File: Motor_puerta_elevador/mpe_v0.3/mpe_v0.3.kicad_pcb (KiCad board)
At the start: 2 copper layers, 99.7 x 109.9 mm, 50 parts, among them J1 IBT2, J10 ENCODER, J11 SERIAL, J12 POWER, J13 MOTOR, J15 -, J16 -, J2 POWER, J3 MOTOR, J4 PROG, J5 IN1, J6 IN2, J7 IN3, J8 IN4, J9 IN5, P1 Power, P2 Analog, P3 Digital, P4 Digital, P6 CONN_01X01, P7 CONN_01X01, SW1 RESET, U1 ATmega3250PA-AU, U2 PC817, U3 PC817, U4 PC817, U5 PC817, U6 PC817, U7 DCDC_StepDown, Y1 16M

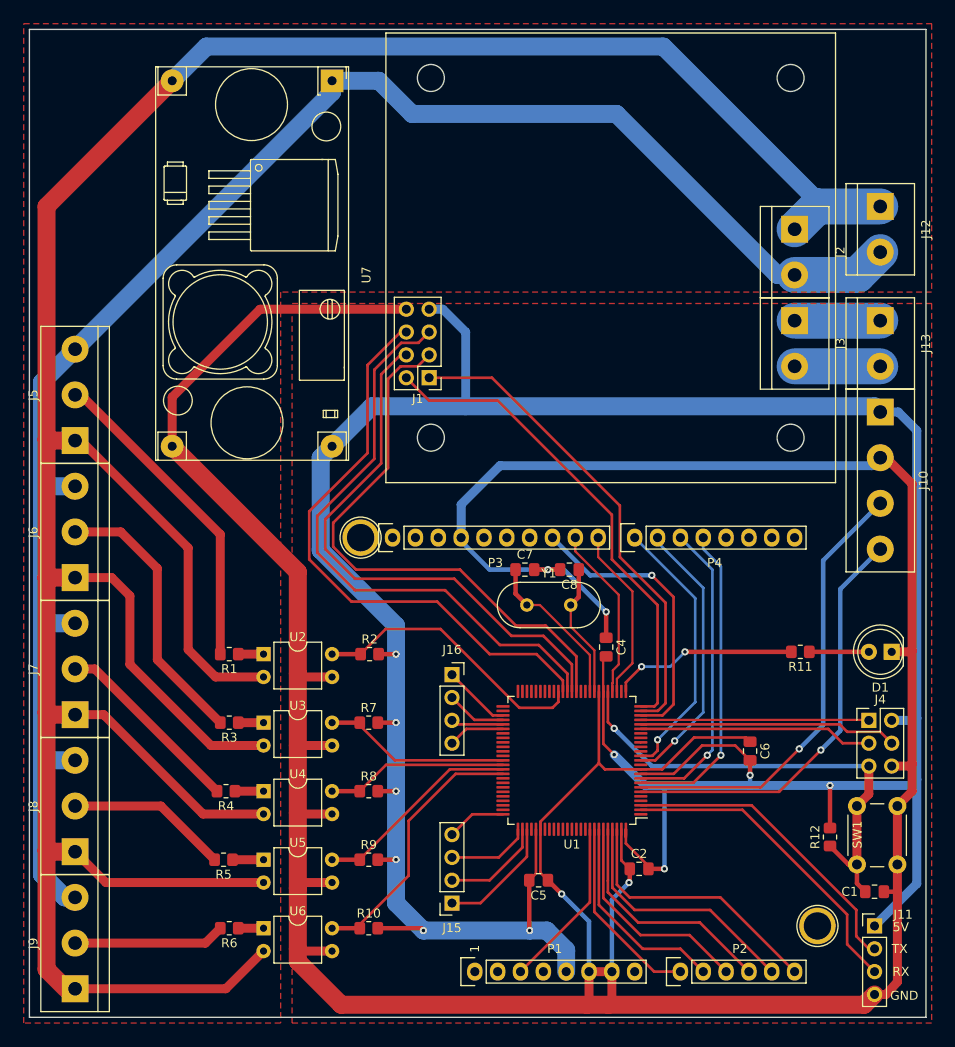
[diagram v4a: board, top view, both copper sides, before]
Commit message: poner zonas relleno
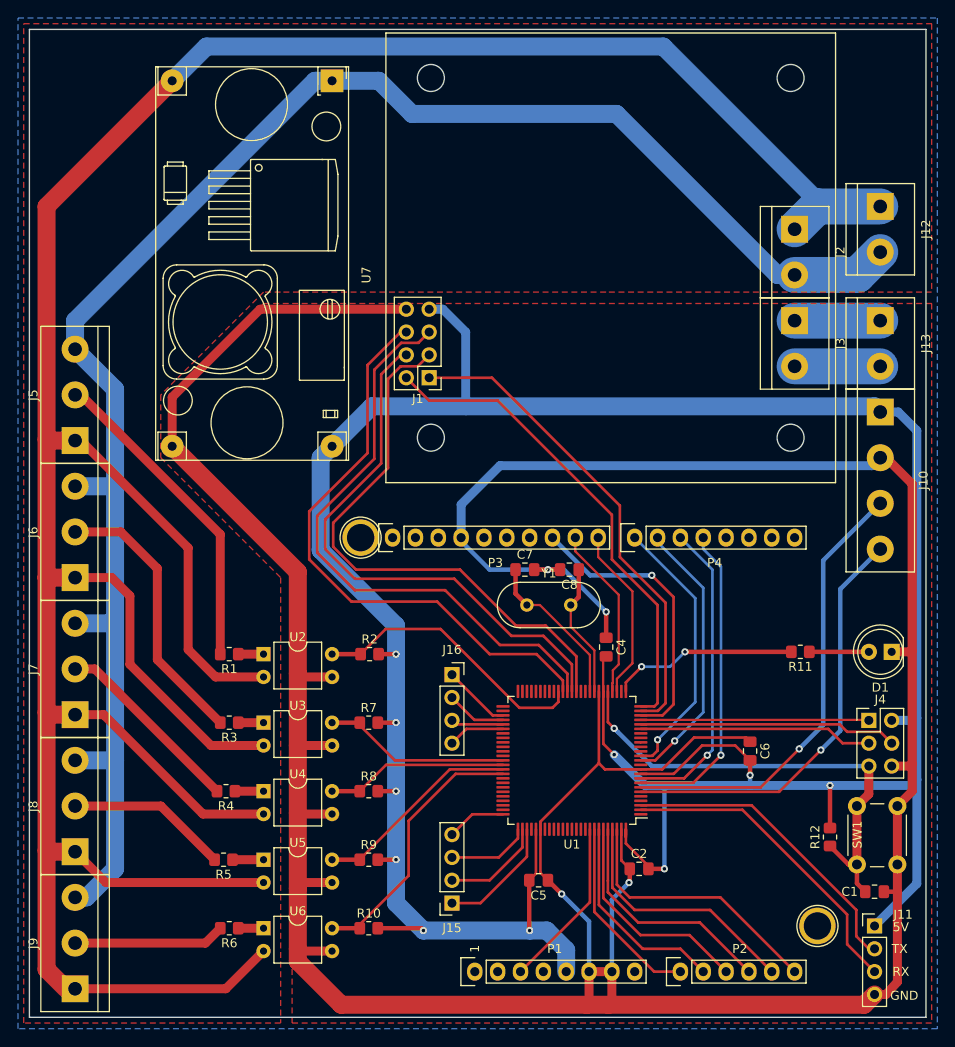
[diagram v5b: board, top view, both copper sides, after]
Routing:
- net +24V: track 188.8 -> 192.7 mm
- added copper zone on B.Cu, net GND
